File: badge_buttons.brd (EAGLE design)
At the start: 160 x 100 mm, 6 parts

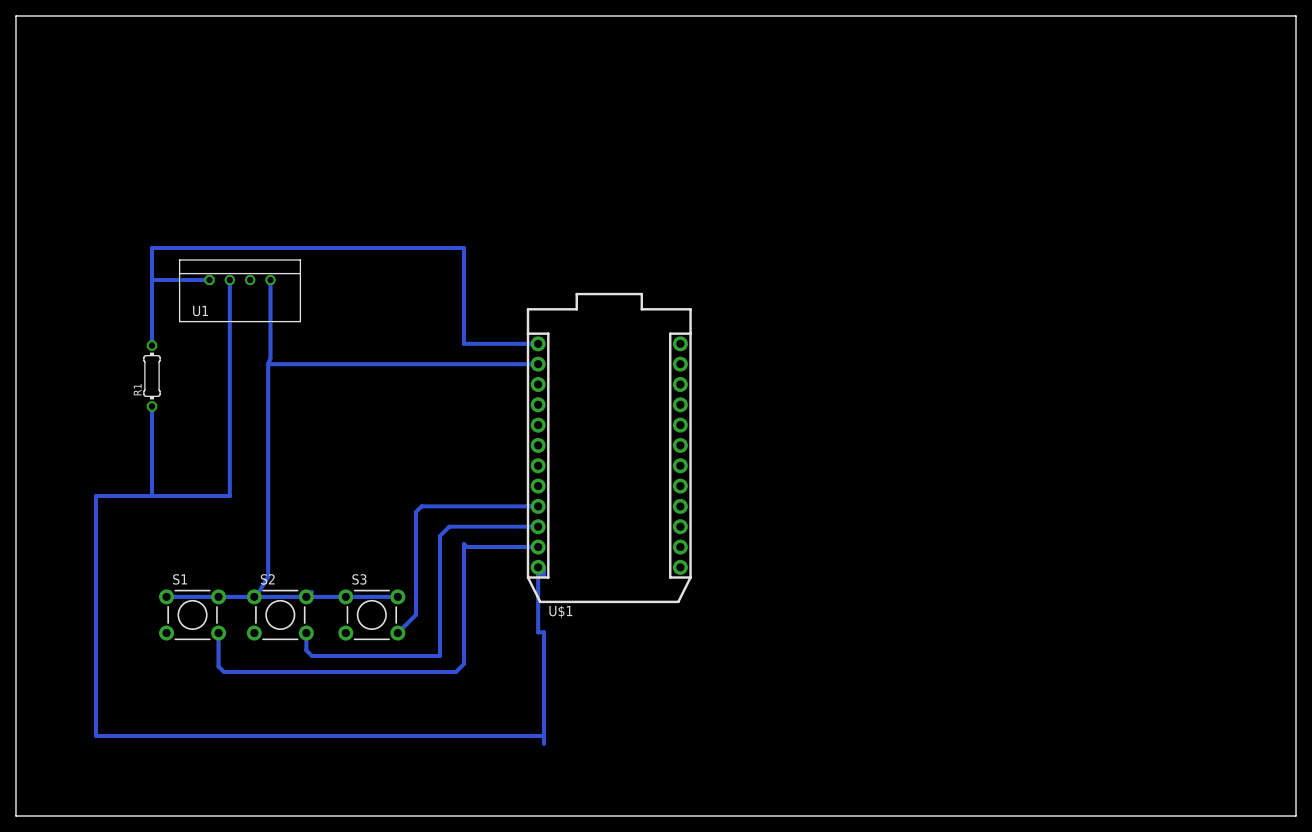
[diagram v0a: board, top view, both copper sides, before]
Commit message: clean up lines, add sensor loop
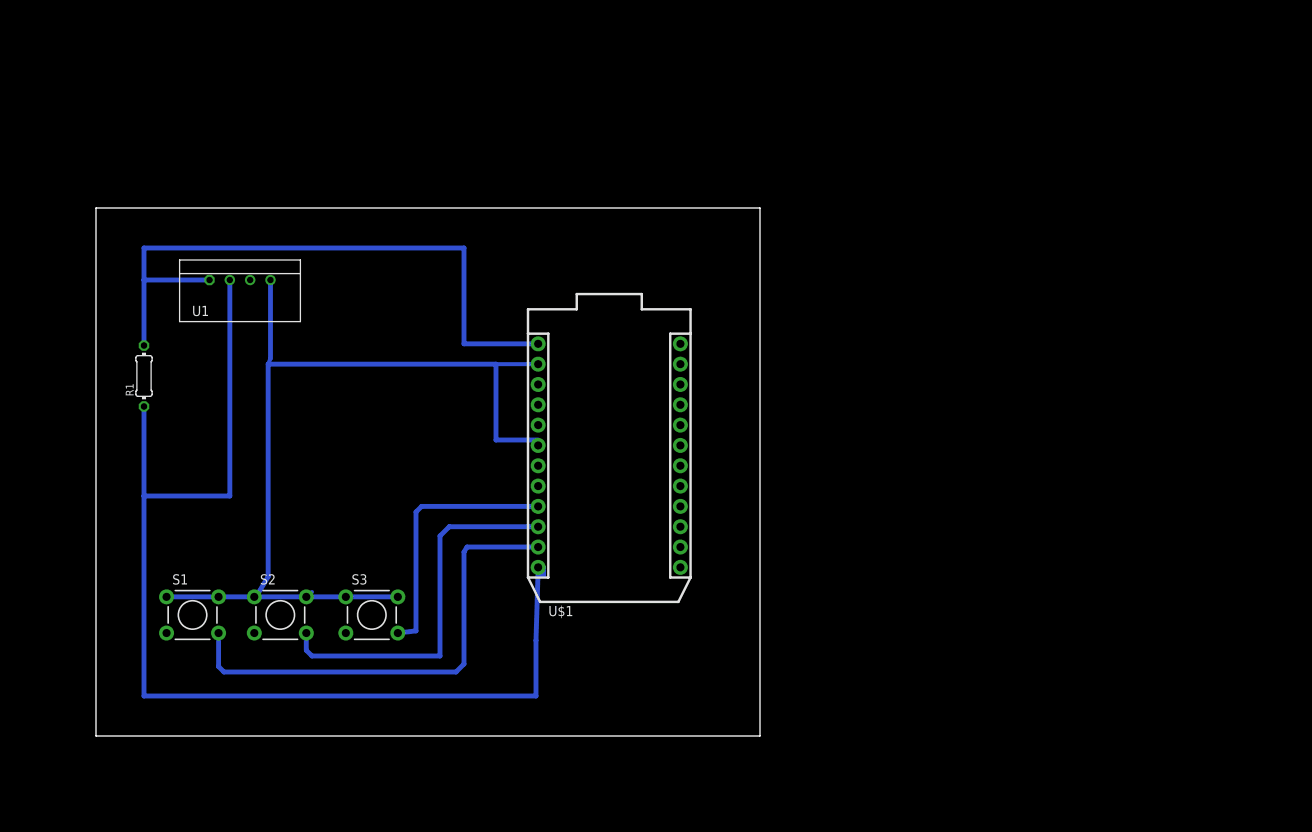
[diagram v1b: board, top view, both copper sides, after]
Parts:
- moved R1 1.00 mm to (16.0, 55.0)
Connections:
- net N$4: now also U$1.6
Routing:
- net N$6: track 165.2 -> 142.2 mm
- net N$4: track 103.7 -> 119.1 mm
- net N$5: track 79.6 -> 81.6 mm
- net N$1: track 32.0 -> 33.1 mm
- net N$3: track 60.0 -> 59.2 mm
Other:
- board size 160 x 100 mm -> 83 x 66 mm
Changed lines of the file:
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@@
 <drawing>
 <settings>
-<setting alwaysvectorfont="yes"/>
+<setting alwaysvectorfont="no"/>
 <setting verticaltext="up"/>
 </settings>
@@
 <board>
 <plain>
-<wire x1="0" y1="0" x2="160" y2="0" width="0" layer="20"/>
-<wire x1="160" y1="0" x2="160" y2="100" width="0" layer="20"/>
-<wire x1="160" y1="100" x2="0" y2="100" width="0" layer="20"/>
-<wire x1="0" y1="100" x2="0" y2="0" width="0" layer="20"/>
+<wire x1="10" y1="10" x2="93" y2="10" width="0" layer="20"/>
+<wire x1="93" y1="10" x2="93" y2="76" width="0" layer="20"/>
+<wire x1="93" y1="76" x2="10" y2="76" width="0" layer="20"/>
+<wire x1="10" y1="76" x2="10" y2="10" width="0" layer="20"/>
 </plain>
 <attributes>
@@
 <param name="TopRouterVariant" value="1"/>
 <param name="tpViaShape" value="round"/>
-<param name="PrefDir.1" value="a"/>
+<param name="PrefDir.1" value="0"/>
 <param name="PrefDir.2" value="0"/>
 <param name="PrefDir.3" value="0"/>
@@
 <attribute name="PROD_ID" value="SEN-10167" x="28" y="67" size="1.778" layer="27" display="off"/>
 </element>
-<element name="R1" library="resistor" library_urn="urn:adsk.eagle:library:348" package="0204/7" package3d_urn="urn:adsk.eagle:package:25945/1" value="" x="17" y="55" rot="R90"/>
+<element name="R1" library="resistor" library_urn="urn:adsk.eagle:library:348" package="0204/7" package3d_urn="urn:adsk.eagle:package:25945/1" value="" x="16" y="55" rot="R90"/>
 </elements>
 <signals>
@@
 <wire x1="65.27" y1="38.7" x2="65" y2="38.97" width="0.3048" layer="16"/>
 <wire x1="65" y1="38.97" x2="65" y2="39" width="0.3048" layer="16"/>
-<wire x1="47.7312" y1="22.8694" x2="50" y2="25.1382" width="0.508" layer="16"/>
-<wire x1="50" y1="25.1382" x2="50" y2="38" width="0.508" layer="16"/>
-<wire x1="50" y1="38" x2="50.7" y2="38.7" width="0.508" layer="16"/>
-<wire x1="50.7" y1="38.7" x2="65.27" y2="38.7" width="0.508" layer="16"/>
+<wire x1="47.7312" y1="22.8694" x2="50" y2="23.1382" width="0.6096" layer="16"/>
+<wire x1="50" y1="23.1382" x2="50" y2="38" width="0.6096" layer="16"/>
+<wire x1="50" y1="38" x2="50.7" y2="38.7" width="0.6096" layer="16"/>
+<wire x1="50.7" y1="38.7" x2="65.27" y2="38.7" width="0.6096" layer="16"/>
 </signal>
 <signal name="N$2">
 <contactref element="S2" pad="4"/>
 <contactref element="U$1" pad="10"/>
-<wire x1="36.2912" y1="22.8694" x2="36.2912" y2="20.7088" width="0.508" layer="16"/>
-<wire x1="36.2912" y1="20.7088" x2="37" y2="20" width="0.508" layer="16"/>
-<wire x1="37" y1="20" x2="53" y2="20" width="0.508" layer="16"/>
-<wire x1="53" y1="20" x2="53" y2="35" width="0.508" layer="16"/>
-<wire x1="54.16" y1="36.16" x2="65.27" y2="36.16" width="0.508" layer="16"/>
-<wire x1="53" y1="35" x2="54.16" y2="36.16" width="0.508" layer="16"/>
+<wire x1="36.2912" y1="22.8694" x2="36.2912" y2="20.7088" width="0.6096" layer="16"/>
+<wire x1="36.2912" y1="20.7088" x2="37" y2="20" width="0.6096" layer="16"/>
+<wire x1="37" y1="20" x2="53" y2="20" width="0.6096" layer="16"/>
+<wire x1="53" y1="20" x2="53" y2="35" width="0.6096" layer="16"/>
+<wire x1="54.16" y1="36.16" x2="65.27" y2="36.16" width="0.6096" layer="16"/>
+<wire x1="53" y1="35" x2="54.16" y2="36.16" width="0.6096" layer="16"/>
 </signal>
 <signal name="N$3">
 <contactref element="S1" pad="4"/>
 <contactref element="U$1" pad="11"/>
-<wire x1="25.3212" y1="22.8694" x2="25.3212" y2="18.6788" width="0.508" layer="16"/>
-<wire x1="25.3212" y1="18.6788" x2="26" y2="18" width="0.508" layer="16"/>
-<wire x1="26" y1="18" x2="55" y2="18" width="0.508" layer="16"/>
-<wire x1="55" y1="18" x2="56" y2="19" width="0.508" layer="16"/>
-<wire x1="56" y1="19" x2="56" y2="34" width="0.508" layer="16"/>
-<wire x1="56" y1="34" x2="56.38" y2="33.62" width="0.508" layer="16"/>
-<wire x1="56.38" y1="33.62" x2="65.27" y2="33.62" width="0.508" layer="16"/>
+<wire x1="25.3212" y1="22.8694" x2="25.3212" y2="18.6788" width="0.6096" layer="16"/>
+<wire x1="25.3212" y1="18.6788" x2="26" y2="18" width="0.6096" layer="16"/>
+<wire x1="26" y1="18" x2="55" y2="18" width="0.6096" layer="16"/>
+<wire x1="55" y1="18" x2="56" y2="19" width="0.6096" layer="16"/>
+<wire x1="56" y1="19" x2="56" y2="33" width="0.6096" layer="16"/>
+<wire x1="56" y1="33" x2="56.38" y2="33.62" width="0.6096" layer="16"/>
+<wire x1="56.38" y1="33.62" x2="65.27" y2="33.62" width="0.6096" layer="16"/>
 </signal>
 <signal name="N$4">
@@
 <contactref element="S2" pad="2"/>
 <contactref element="S3" pad="2"/>
-<wire x1="18.8188" y1="27.3906" x2="25.3212" y2="27.3906" width="0.508" layer="16"/>
-<wire x1="25.3212" y1="27.3906" x2="29.7888" y2="27.3906" width="0.508" layer="16"/>
+<wire x1="18.8188" y1="27.3906" x2="25.3212" y2="27.3906" width="0.6096" layer="16"/>
+<wire x1="25.3212" y1="27.3906" x2="29.7888" y2="27.3906" width="0.6096" layer="16"/>
 <wire x1="29.7888" y1="27.3906" x2="30" y2="27.3906" width="0.508" layer="16"/>
-<wire x1="30" y1="27.3906" x2="36.2912" y2="27.3906" width="0.508" layer="16"/>
+<wire x1="30" y1="27.3906" x2="36.2912" y2="27.3906" width="0.6096" layer="16"/>
 <wire x1="37" y1="28" x2="36.3906" y2="27.3906" width="0.508" layer="16"/>
 <wire x1="36.3906" y1="27.3906" x2="36.2912" y2="27.3906" width="0.508" layer="16"/>
-<wire x1="36.2912" y1="27.3906" x2="41.2288" y2="27.3906" width="0.508" layer="16"/>
-<wire x1="41.2288" y1="27.3906" x2="47.7312" y2="27.3906" width="0.508" layer="16"/>
-<wire x1="31.81" y1="67" x2="31.81" y2="57.19" width="0.508" layer="16"/>
-<wire x1="31.52" y1="56.48" x2="65.27" y2="56.48" width="0.508" layer="16"/>
+<wire x1="36.2912" y1="27.3906" x2="41.2288" y2="27.3906" width="0.6096" layer="16"/>
+<wire x1="41.2288" y1="27.3906" x2="47.7312" y2="27.3906" width="0.6096" layer="16"/>
+<wire x1="31.81" y1="67" x2="31.81" y2="57.19" width="0.6096" layer="16"/>
 <wire x1="31.81" y1="57.19" x2="31.52" y2="56.48" width="0.508" layer="16"/>
-<wire x1="31.52" y1="56.48" x2="31.52" y2="29.9106" width="0.508" layer="16"/>
-<wire x1="31.52" y1="29.9106" x2="30" y2="27.3906" width="0.508" layer="16"/>
+<wire x1="31.52" y1="56.48" x2="31.52" y2="29.9106" width="0.6096" layer="16"/>
+<wire x1="31.52" y1="29.9106" x2="30" y2="27.3906" width="0.6096" layer="16"/>
+<contactref element="U$1" pad="6"/>
+<wire x1="65.27" y1="56.48" x2="60" y2="56.48" width="0.508" layer="16"/>
+<wire x1="60" y1="56.48" x2="31.52" y2="56.48" width="0.6096" layer="16"/>
+<wire x1="65.27" y1="46.32" x2="65.27" y2="47" width="0.508" layer="16"/>
+<wire x1="65.27" y1="47" x2="60" y2="47" width="0.6096" layer="16"/>
+<wire x1="60" y1="47" x2="60" y2="56.48" width="0.6096" layer="16"/>
 </signal>
 <signal name="N$5">
@@
 <contactref element="U$1" pad="1"/>
 <contactref element="R1" pad="2"/>
-<wire x1="24.19" y1="67" x2="17" y2="67" width="0.508" layer="16"/>
-<wire x1="17" y1="67" x2="17" y2="71" width="0.508" layer="16"/>
-<wire x1="17" y1="71" x2="56" y2="71" width="0.508" layer="16"/>
-<wire x1="56" y1="71" x2="56" y2="59.02" width="0.508" layer="16"/>
-<wire x1="56" y1="59.02" x2="65.27" y2="59.02" width="0.508" layer="16"/>
-<wire x1="17" y1="67" x2="17" y2="58.81" width="0.508" layer="16"/>
+<wire x1="24.19" y1="67" x2="16" y2="67" width="0.6096" layer="16"/>
+<wire x1="16" y1="67" x2="16" y2="71" width="0.6096" layer="16"/>
+<wire x1="16" y1="71" x2="56" y2="71" width="0.6096" layer="16"/>
+<wire x1="56" y1="71" x2="56" y2="59.02" width="0.6096" layer="16"/>
+<wire x1="56" y1="59.02" x2="65.27" y2="59.02" width="0.6096" layer="16"/>
+<wire x1="16" y1="67" x2="16" y2="58.81" width="0.6096" layer="16"/>
 </signal>
 <signal name="N$6">
@@
 <contactref element="U$1" pad="12"/>
 <contactref element="R1" pad="1"/>
-<wire x1="26.73" y1="67" x2="26.73" y2="40" width="0.508" layer="16"/>
-<wire x1="26.73" y1="40" x2="17" y2="40" width="0.508" layer="16"/>
-<wire x1="17" y1="40" x2="10" y2="40" width="0.508" layer="16"/>
-<wire x1="10" y1="40" x2="10" y2="10" width="0.508" layer="16"/>
-<wire x1="10" y1="10" x2="66" y2="10" width="0.508" layer="16"/>
-<wire x1="66" y1="10" x2="66" y2="9" width="0.508" layer="16"/>
+<wire x1="26.73" y1="67" x2="26.73" y2="40" width="0.6096" layer="16"/>
+<wire x1="26.73" y1="40" x2="16" y2="40" width="0.6096" layer="16"/>
+<wire x1="16" y1="40" x2="16" y2="15" width="0.6096" layer="16"/>
+<wire x1="16" y1="15" x2="65" y2="15" width="0.6096" layer="16"/>
 <wire x1="66" y1="31.08" x2="65.27" y2="31.08" width="0.508" layer="16"/>
-<wire x1="66" y1="10" x2="66" y2="22.952" width="0.508" layer="16"/>
-<wire x1="66" y1="22.952" x2="65.27" y2="22.952" width="0.508" layer="16"/>
-<wire x1="65.27" y1="22.952" x2="65.27" y2="30.064" width="0.508" layer="16"/>
+<wire x1="65" y1="15" x2="65" y2="21.952" width="0.6096" layer="16"/>
+<wire x1="65" y1="21.952" x2="65.27" y2="30.952" width="0.6096" layer="16"/>
+<wire x1="65.27" y1="30.952" x2="65.27" y2="30.064" width="0.508" layer="16"/>
 <wire x1="65.27" y1="30.064" x2="66" y2="30.064" width="0.508" layer="16"/>
 <wire x1="66" y1="30.064" x2="66" y2="31.08" width="0.508" layer="16"/>
-<wire x1="17" y1="51.19" x2="17" y2="40" width="0.508" layer="16"/>
+<wire x1="16" y1="51.19" x2="16" y2="40" width="0.6096" layer="16"/>
 </signal>
 </signals>
